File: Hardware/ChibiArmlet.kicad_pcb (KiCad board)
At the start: 2 copper layers, 115 x 16 mm, 56 parts, among them M1 MOTOR_PAD, Q1 MMBT2222, Q2 MMBT2222, Q3 LED_RGB 5050

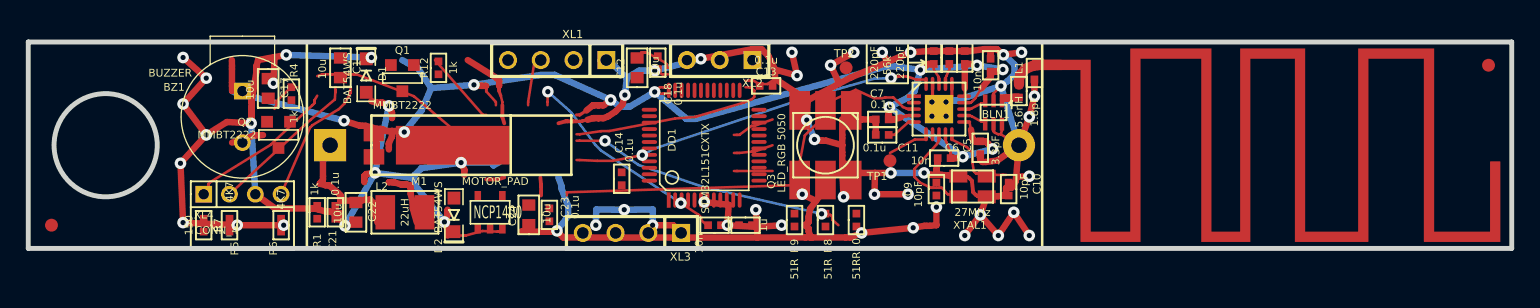
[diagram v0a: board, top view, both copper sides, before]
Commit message: Hardware: * Pill connector now 2.54mm, placed near battery
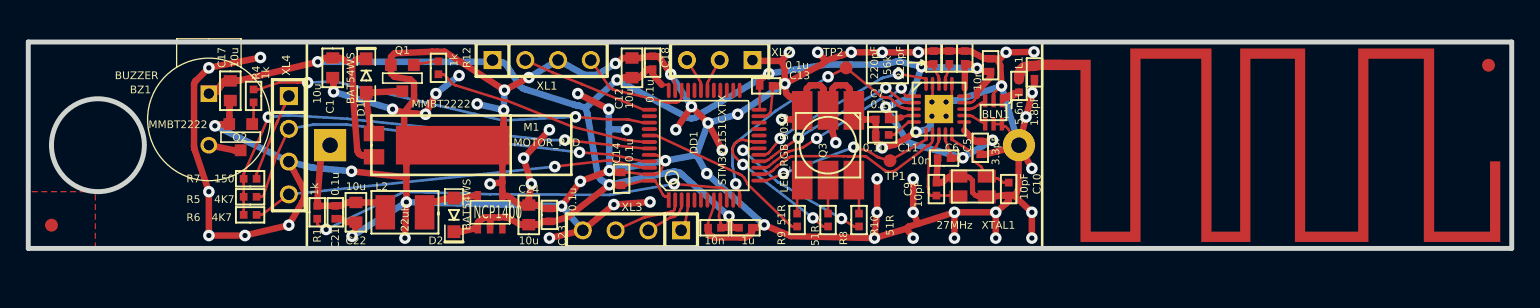
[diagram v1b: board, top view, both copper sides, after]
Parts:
- XL4: footprint CONN_PBS2_04R -> SIL-4
- moved XL4 5.23 mm to (179.2, 181.0), turned to 270 degrees
- moved R7 5.09 mm to (176.2, 183.6), turned to 180 degrees
- moved Q2 2.94 mm to (175.5, 180.4)
- moved R4 2.94 mm to (176.5, 177.2)
- moved C17 2.94 mm to (174.7, 176.8)
- moved R5 2.72 mm to (176.2, 185.0), turned to 180 degrees
- moved BZ1 2.61 mm to (173.0, 179.0)
- moved R6 2.53 mm to (176.2, 186.4), turned to 180 degrees
- moved XL1 1.20 mm to (198.8, 174.4), turned to 0 degrees
- moved C1 0.60 mm to (182.6, 175.0)
- moved C18 0.40 mm to (207.4, 174.6)
- moved L1 0.40 mm to (235.8, 176.4)
- moved C12 0.40 mm to (205.8, 175.0)
- moved C15 0.20 mm to (212.2, 187.4)
- moved C16 0.20 mm to (214.6, 187.4)
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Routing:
- net GND: track 150.5 -> 364.7 mm, vias 21 -> 71
- net N-0000036: track 50.5 -> 2.46 mm, vias 8 -> 0
- net +3.3V: track 207.0 -> 164.3 mm, vias 31 -> 10
- net (no net): track 38.9 -> 0.00 mm
- net /PeriphPwr: track 0.00 -> 37.6 mm, vias 0 -> 2
- net N-0000021: track 0.00 -> 33.8 mm, vias 0 -> 2
- net /Buzzer: track 2.62 -> 31.2 mm, vias 0 -> 2
- net N-000003: track 27.3 -> 2.60 mm, vias 2 -> 0
- net /P_SCL: track 11.9 -> 34.3 mm, vias 0 -> 1
- net N-0000037: track 24.7 -> 3.80 mm, vias 5 -> 0
- net /P_SDA: track 10.3 -> 31.2 mm, vias 0 -> 1
- net N-000004: track 23.0 -> 2.66 mm, vias 1 -> 0
- net /Vibro: track 0.00 -> 17.4 mm
- net /CC_GDO2: track 4.98 -> 21.3 mm, vias 0 -> 2
- net /CC_CS: track 0.00 -> 15.6 mm
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- added copper zone on B.Cu, net GND
- added copper zone on F.Cu, net GND
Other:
- outline, holes or cut-outs redrawn

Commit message: Hardware v3, sent to pilot production
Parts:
- XL4: footprint SIL-4 -> CONN_PBS_4R
- moved R6 28.4 mm to (204.4, 183.0)
- moved R5 28.4 mm to (204.4, 181.8)
- moved R7 28.4 mm to (204.4, 180.6), turned to 0 degrees
- moved R4 28.0 mm to (204.4, 178.2), turned to 180 degrees
- moved D1 16.6 mm to (171.5, 185.0)
- moved XL4 16.3 mm to (195.4, 179.0), turned to 0 degrees
- moved Q1 14.8 mm to (173.2, 175.0)
- moved R12 14.3 mm to (204.4, 179.4), turned to 180 degrees
- moved DA1 13.6 mm to (185.8, 176.0), turned to 180 degrees
- moved C23 13.4 mm to (192.0, 175.2), turned to 270 degrees
- moved M1 13.2 mm to (173.0, 185.0)
- moved C24 13.1 mm to (190.4, 175.6), turned to 270 degrees
- moved R1 11.5 mm to (182.6, 174.8), turned to 0 degrees
- moved D2 10.8 mm to (188.6, 176.2), turned to 270 degrees
- moved C22 10.0 mm to (182.2, 176.4), turned to 180 degrees
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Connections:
- M1 pad 1: +3.3V -> /VibroOut
- M1 pad 2: /VibroOut -> +3.3V
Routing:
- net /PeriphPwr: track 37.6 -> 5.59 mm, vias 2 -> 0
- net N-0000027: track 1.94 -> 30.8 mm, vias 0 -> 2
- net /Buzzer: track 31.2 -> 2.62 mm, vias 2 -> 0
- net N-0000012: track 1.70 -> 29.9 mm, vias 0 -> 2
- net +3.3V: track 164.3 -> 144.5 mm, vias 10 -> 9
- net /P_SCL: track 34.3 -> 14.5 mm
- net /P_SDA: track 31.2 -> 11.9 mm
- net GND: track 364.7 -> 381.5 mm, vias 71 -> 66
- net /Vibro: track 17.4 -> 2.84 mm
- net /VibroOut: track 6.13 -> 13.5 mm
- net /PeriphPwr1: track 6.92 -> 12.6 mm
- net N-0000021: track 33.8 -> 35.9 mm
- net +BATT: track 10.7 -> 9.74 mm
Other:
- board size 115 x 16 mm -> 114 x 16 mm
- rule trace_min: 0.1 -> 0.2
- rule via_min_size: 0.889 -> 0.9

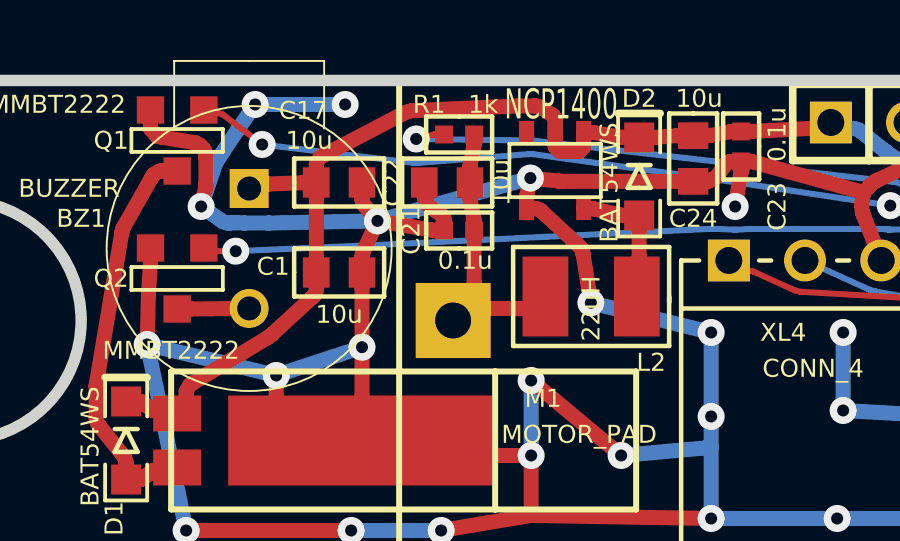
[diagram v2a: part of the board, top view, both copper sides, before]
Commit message: * Vibro disconnected from 3V3, connected to Vbat. * BOM renewed
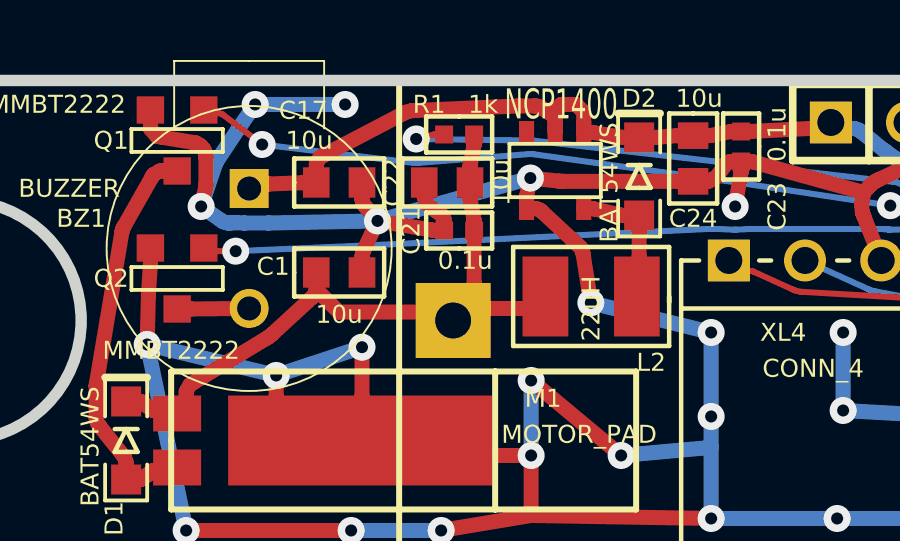
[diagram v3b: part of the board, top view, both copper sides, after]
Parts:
- moved RP1 110.7 mm to (162.0, 187.0)
- moved RP2 110.7 mm to (272.0, 175.0)
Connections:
- C1 pad 1: +3.3V -> +BATT
- D1 pad C: +3.3V -> +BATT
- M1 pad 2: +3.3V -> +BATT
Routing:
- net +BATT: track 9.74 -> 24.1 mm
- net +3.3V: track 144.5 -> 133.1 mm
- net GND: track 381.5 -> 379.0 mm
